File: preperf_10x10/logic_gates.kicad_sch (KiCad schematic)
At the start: 28 parts, among them J4 Conn_01x01_Pin, J5 Conn_01x01_Pin, J6 Conn_01x01_Pin, J7 Conn_01x01_Pin, J8 Conn_01x01_Pin, J9 Conn_01x01_Pin, SW1 SW_DIP_x06, U2 74LS08, U3 74LS32, U4 74LS04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

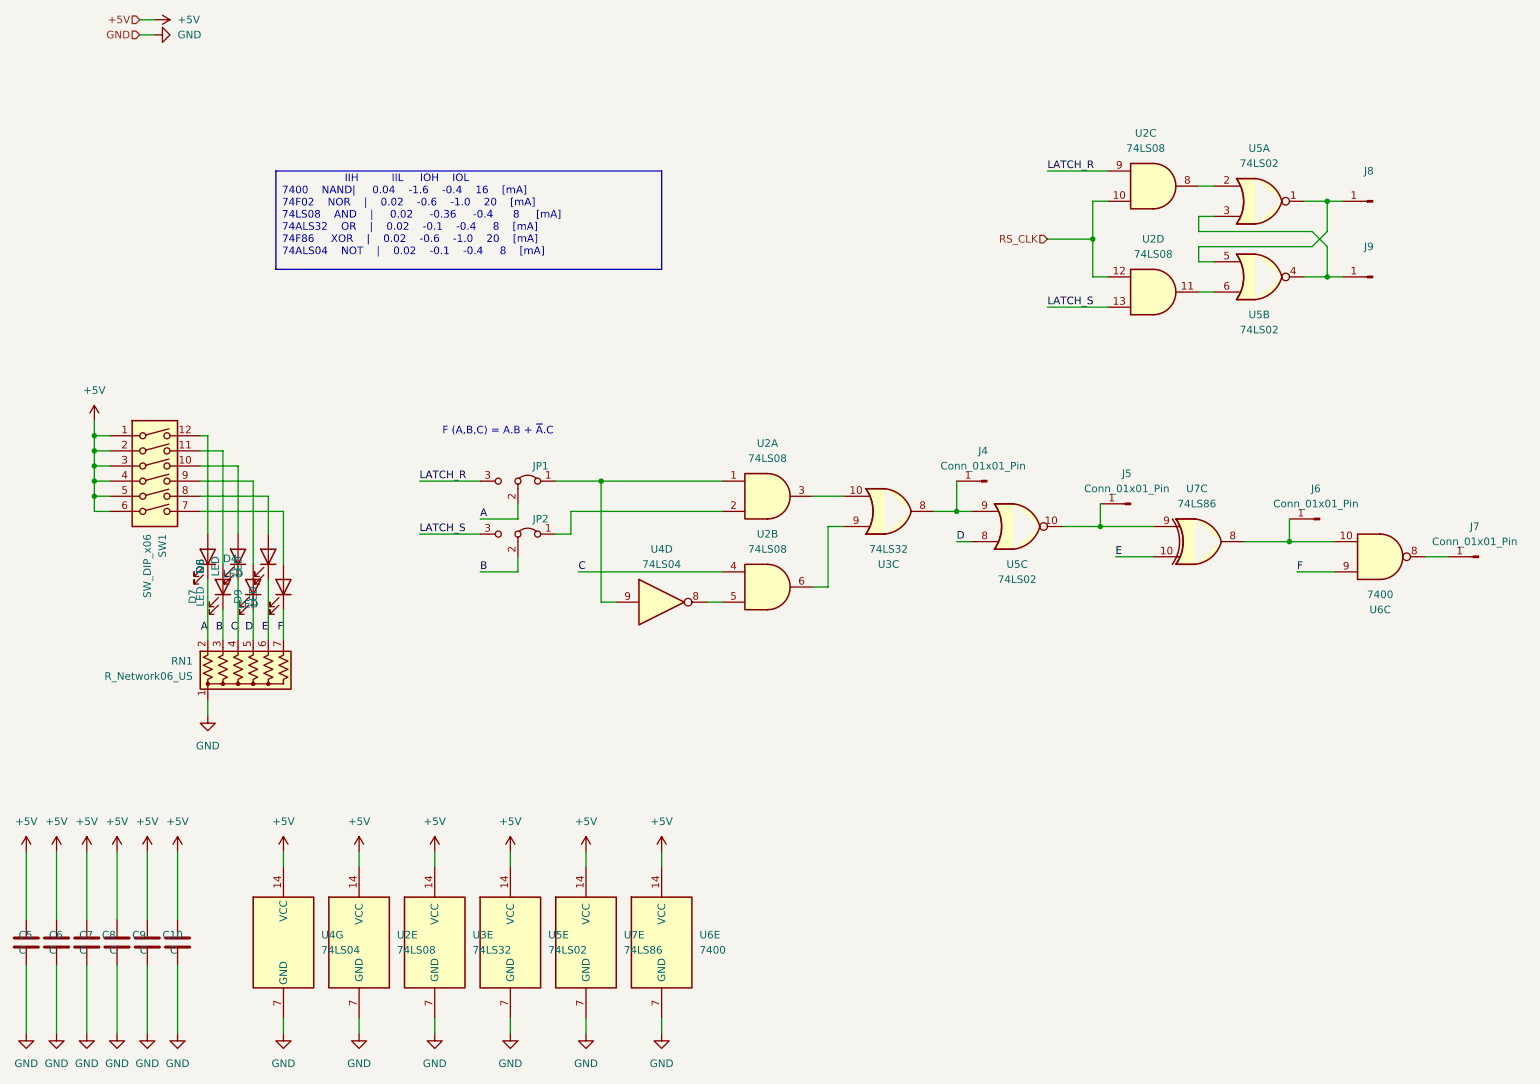
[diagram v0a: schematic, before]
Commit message: [ADD] Digital Logic Design project (FIUBA): PCB implementation of schmitt triggers, logic functions, counters, state machines, and logic probes
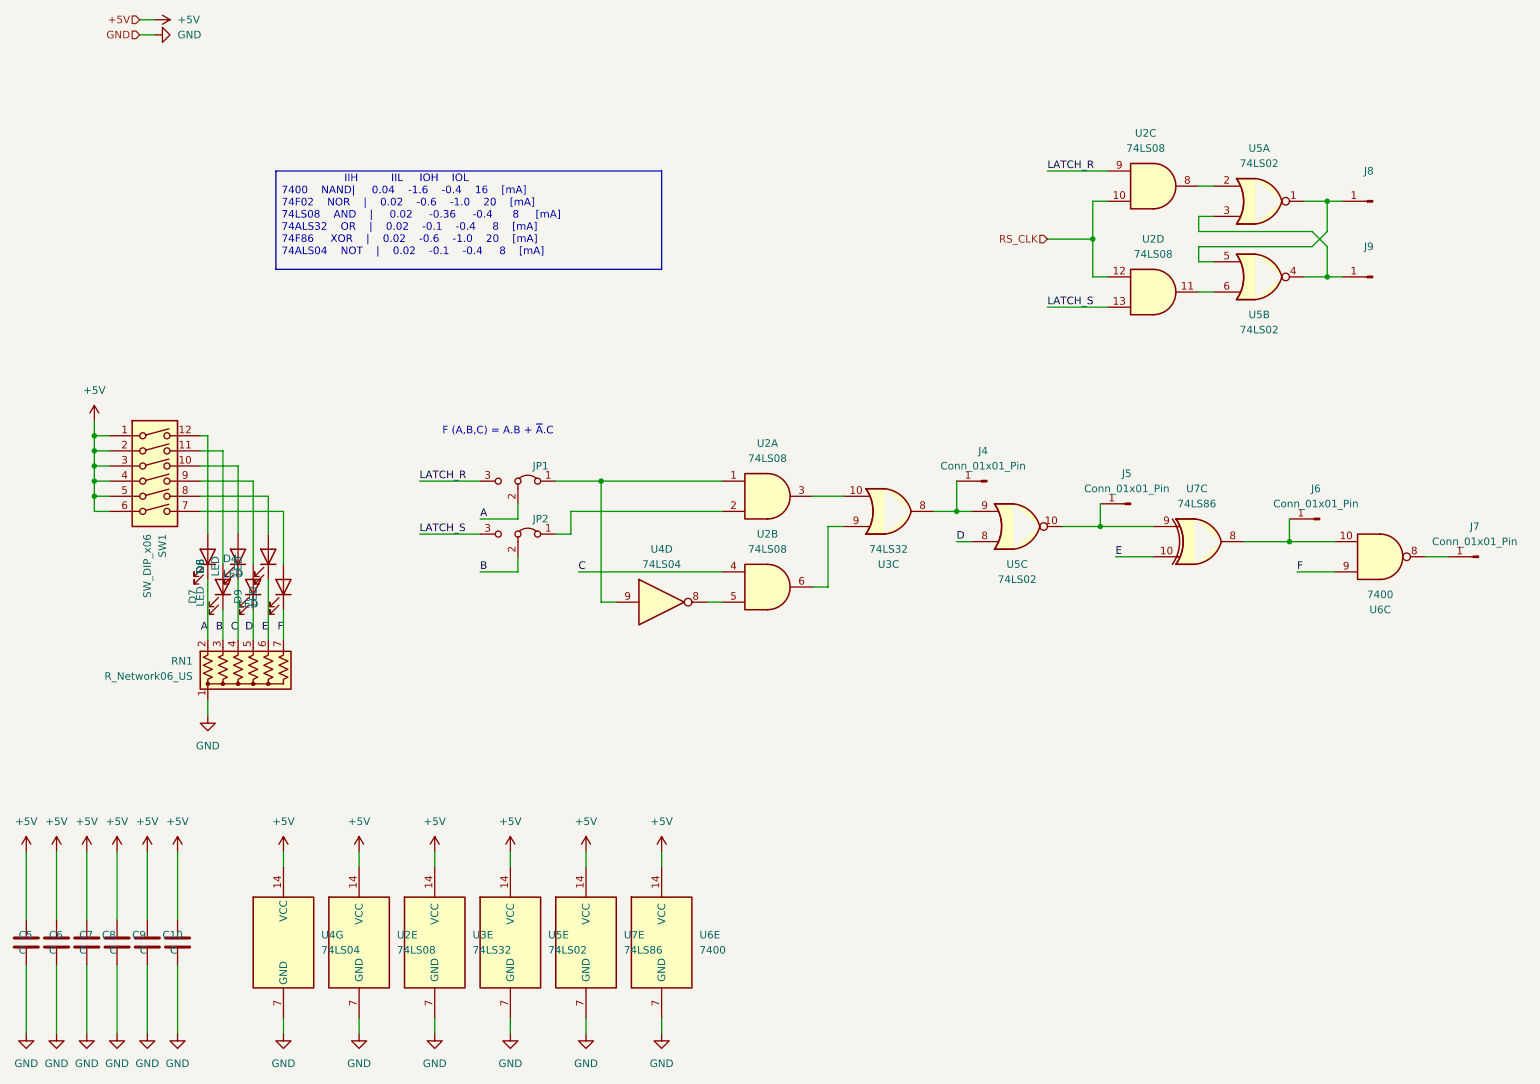
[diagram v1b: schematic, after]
